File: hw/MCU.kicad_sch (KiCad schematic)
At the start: 14 parts, among them J2 Conn_01x06, SW2 SKRPACE010, SW3 SKRPACE010, U2 N32L406RBL7

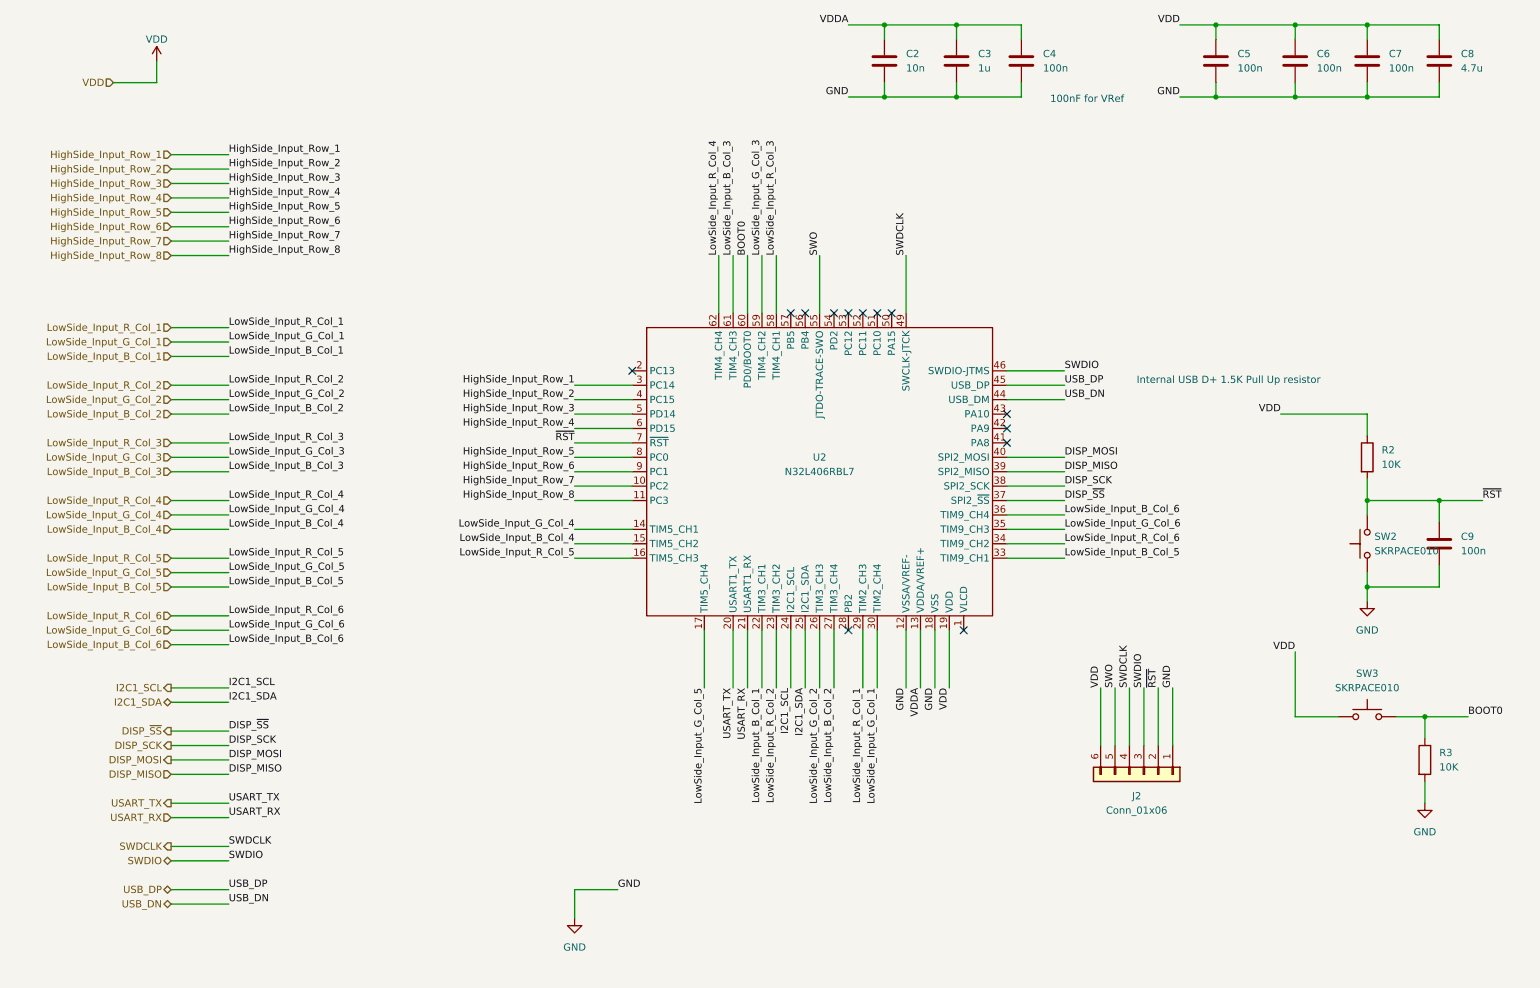
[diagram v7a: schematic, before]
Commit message: changed connections and ports
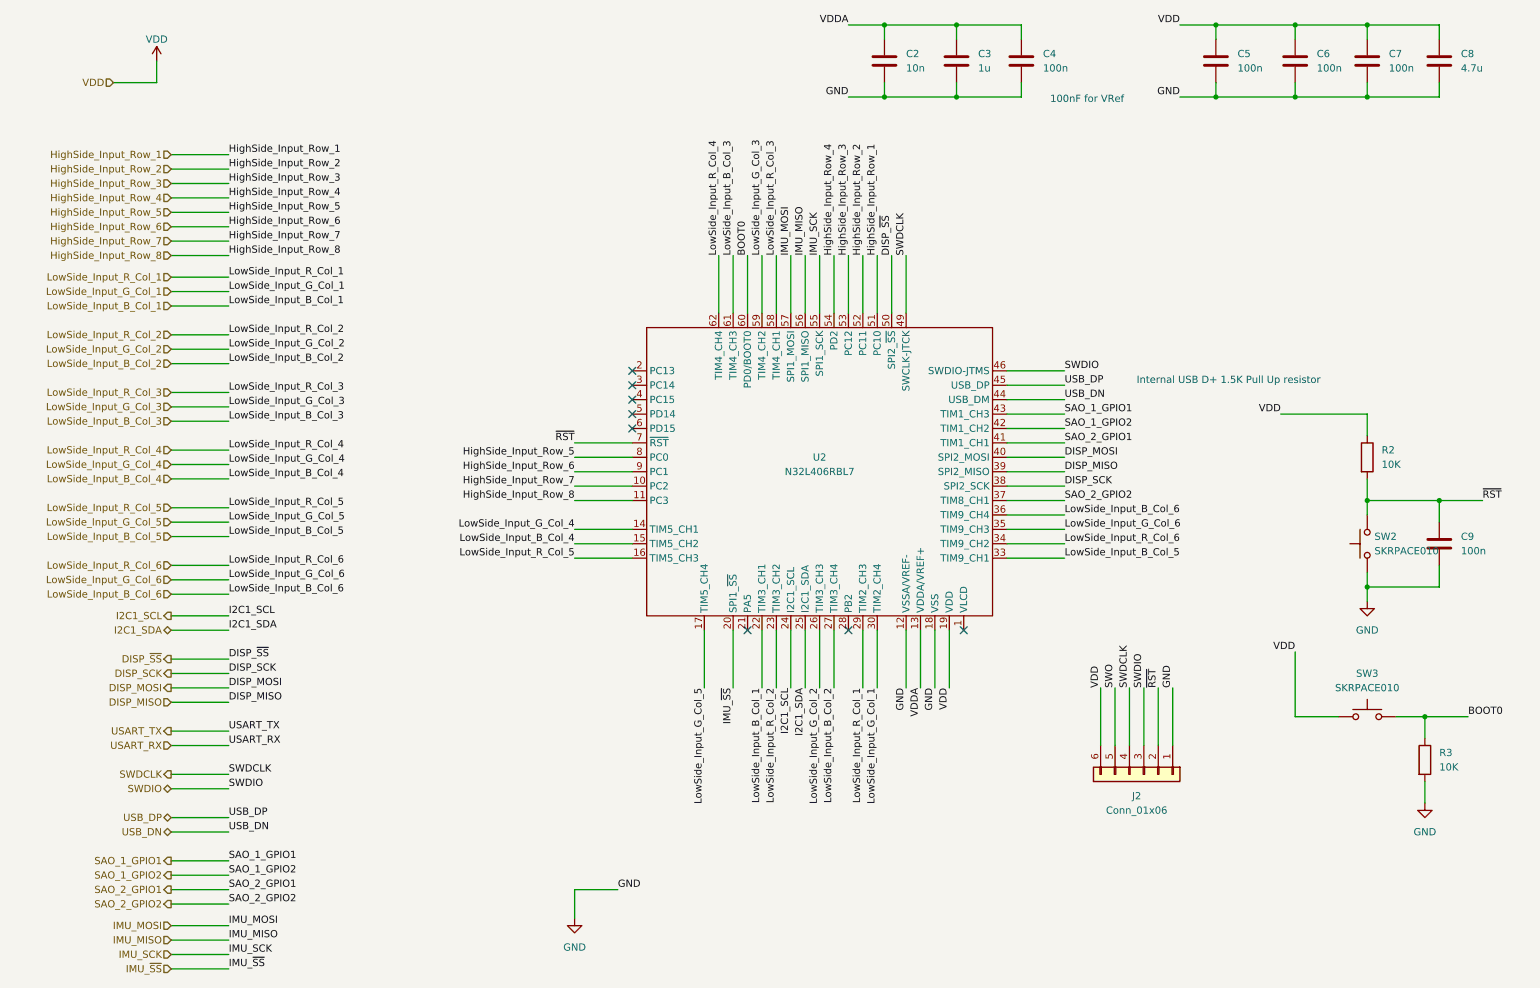
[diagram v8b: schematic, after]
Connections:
- net DISP_~{SS}: now also U2.50 (PA15); no longer U2.37 (PC6)
- net HighSide_Input_Row_1: now also U2.51 (PC10); no longer U2.3 (PC14)
- net HighSide_Input_Row_2: now also U2.52 (PC11); no longer U2.4 (PC15)
- net HighSide_Input_Row_3: now also U2.53 (PC12); no longer U2.5 (PD14)
- net HighSide_Input_Row_4: now also U2.54 (PD2); no longer U2.6 (PD15)
- net SWO: no longer U2.55 (PB3)
- net USART_RX: no longer U2.21 (PA5)
- net USART_TX: no longer U2.20 (PA4)
- net SAO_2_GPIO1: now reaches U2.41 (PA8)
- net SAO_1_GPIO2: now reaches U2.42 (PA9)
- net SAO_1_GPIO1: now reaches U2.43 (PA10)
- net IMU_MISO: now reaches U2.56 (PB4)
- net IMU_MOSI: now reaches U2.57 (PB5)
- new net IMU_SCK: U2.55 (PB3)
- new net IMU_~{SS}: U2.20 (PA4)
- new net SAO_2_GPIO2: U2.37 (PC6)
- no-connect marks 13 -> 8
